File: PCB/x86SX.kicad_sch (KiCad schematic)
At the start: 1 part

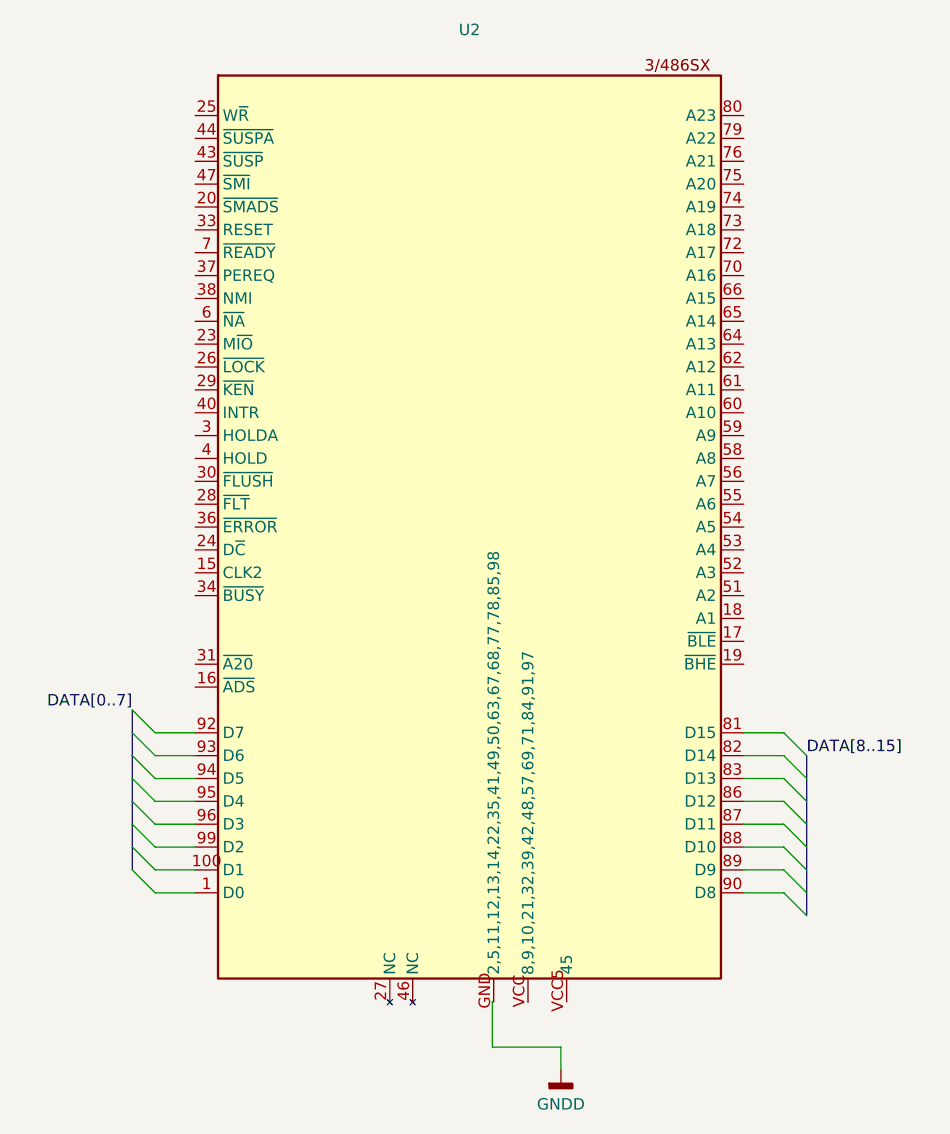
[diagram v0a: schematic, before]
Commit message: broken 386 symbol
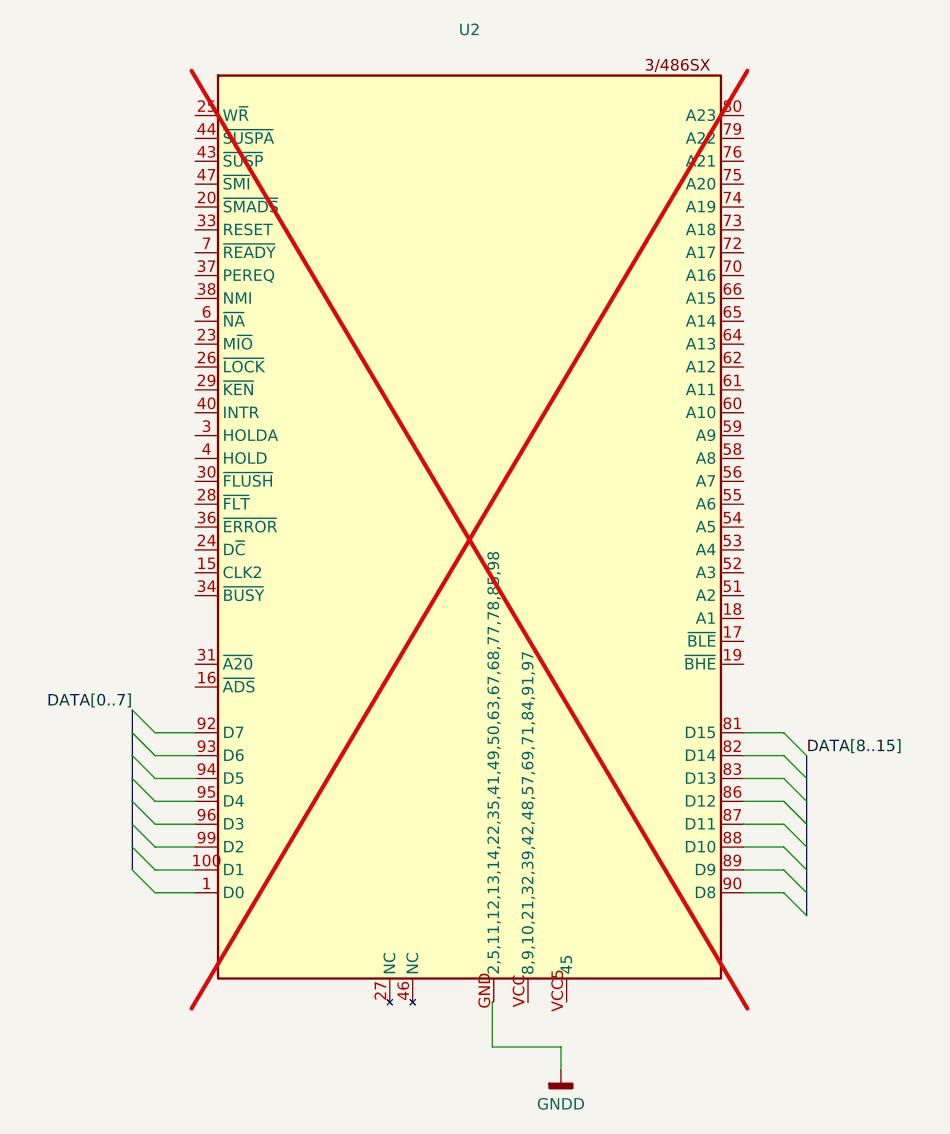
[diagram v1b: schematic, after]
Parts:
- U2: now not fitted; now left out of the parts list
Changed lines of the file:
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@@
 		(unit 1)
 		(body_style 1)
-		(exclude_from_sim no)
-		(in_bom yes)
-		(on_board yes)
-		(in_pos_files yes)
-		(dnp no)
+		(exclude_from_sim yes)
+		(in_bom no)
+		(on_board no)
+		(in_pos_files no)
+		(dnp yes)
 		(fields_autoplaced yes)
 		(property "Reference" "U2"
